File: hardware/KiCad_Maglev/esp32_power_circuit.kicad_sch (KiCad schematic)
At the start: 9 parts

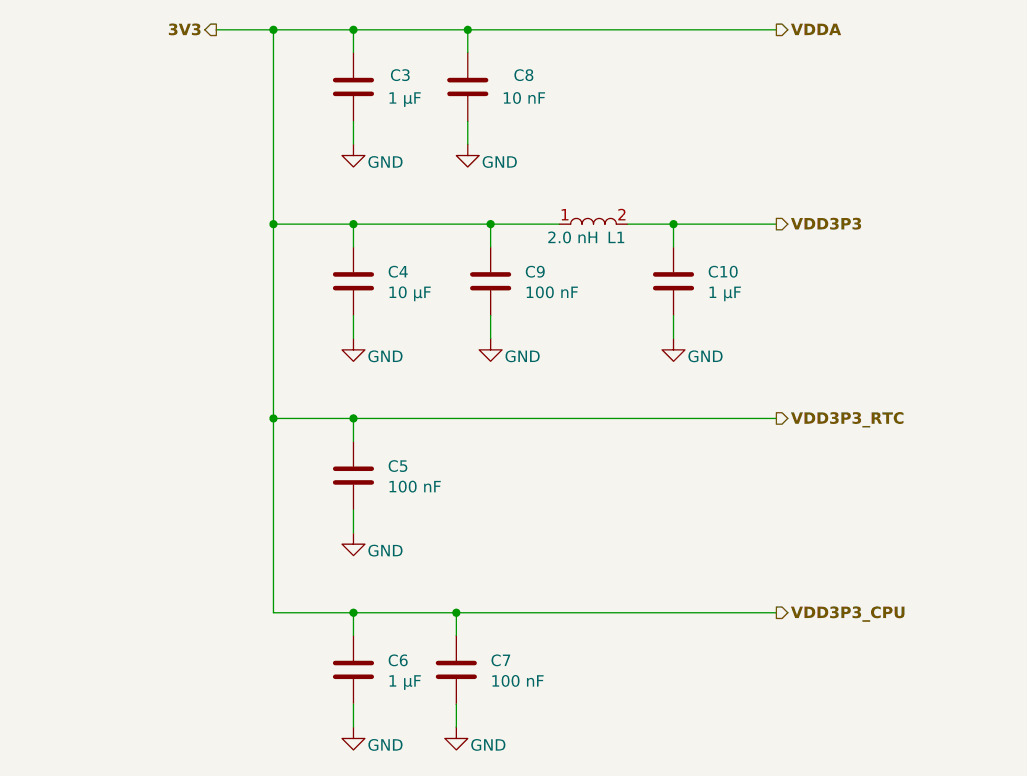
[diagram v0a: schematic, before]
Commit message: Added Footprints/Models for coil and ringmagnet, changed most components to 1206 series
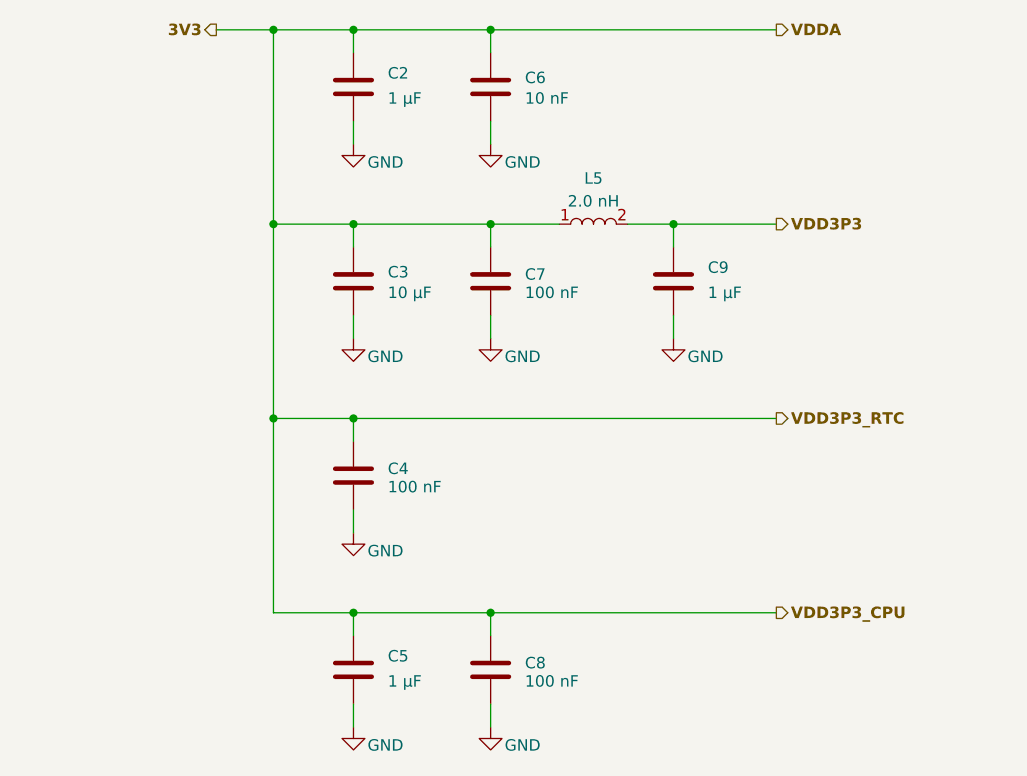
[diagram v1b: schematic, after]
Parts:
- removed C10, C3, C6: 0805_H1.25_R_885012107015, Capacitor_SMD_Wurth:C_Wurth_WCAP-CSGP-0805_H1.25_R, symbol Capacitor_Wurth_WCAP-CSGP:0805_H1.25_R_885012107015
- removed C5, C7, C9: 1812_H1.25_885012210008, Capacitor_SMD_Wurth:C_Wurth_WCAP-CSGP-1812_H1.25, symbol Capacitor_Wurth_WCAP-CSGP:1812_H1.25_885012210008
- removed C8: 0402_885012205050, Capacitor_SMD_Wurth:C_Wurth_WCAP-CSGP-0402, symbol Capacitor_Wurth_WCAP-CSGP:0402_885012205050
- removed L1: 0402_744765020A, Inductor_SMD_Wurth:L_Wurth_WE-KI-0402, symbol Inductor_Wurth_WE-KI:0402_744765020A
- added C2, C5, C9: 1206_H1.6_885012208093, Capacitor_SMD_Wurth:C_Wurth_WCAP-CSGP-1206_H1.6, symbol Capacitor_Wurth_WCAP-CSGP:1206_H1.6_885012208093
- added C4, C7, C8: 1206_H1.25_885012208118, Capacitor_SMD_Wurth:C_Wurth_WCAP-CSGP-1206_H1.25, symbol Capacitor_Wurth_WCAP-CSGP:1206_H1.25_885012208118
- added C6: 1206_H1.25_885012008055, Capacitor_SMD_Wurth:C_Wurth_WCAP-CSGP-1206_H1.25, symbol Capacitor_Wurth_WCAP-CSGP:1206_H1.25_885012008055
- added L5: 0603_744761020A, Inductor_SMD_Wurth:L_Wurth_WE-KI-0603, symbol Inductor_Wurth_WE-KI:0603_744761020A
- renumbered C4 to C3
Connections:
- net 3V3: now also C2.1, C4.1, C5.1, C6.1, C7.1, C8.1, L5.1
- net GND: now also C2.2, C4.2, C5.2, C6.2, C7.2, C8.2, C9.2
- net VDD3P3: now also C9.1, L5.2

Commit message: changed mounting and spacing system and  some detail changes
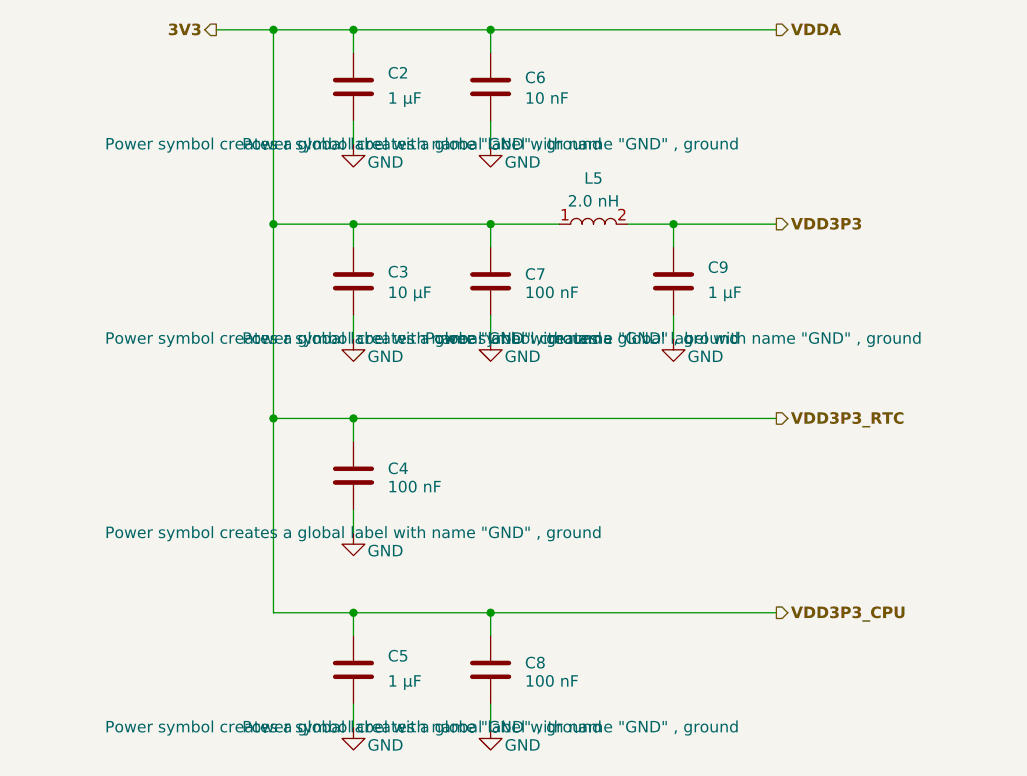
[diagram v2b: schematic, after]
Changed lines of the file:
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@@
 			)
 		)
-		(property "Description" ""
+		(property "Description" "Power symbol creates a global label with name \"GND\" , ground"
 			(at 168.91 91.44 0)
 			(show_name no)
@@
 			)
 		)
-		(property "Description" ""
+		(property "Description" "Power symbol creates a global label with name \"GND\" , ground"
 			(at 148.59 134.62 0)
 			(show_name no)
@@
 			)
 		)
-		(property "Description" ""
+		(property "Description" "Power symbol creates a global label with name \"GND\" , ground"
 			(at 133.35 91.44 0)
 			(show_name no)
@@
 			)
 		)
-		(property "Description" ""
+		(property "Description" "Power symbol creates a global label with name \"GND\" , ground"
 			(at 148.59 69.85 0)
 			(show_name no)
@@
 			)
 		)
-		(property "Description" ""
+		(property "Description" "Power symbol creates a global label with name \"GND\" , ground"
 			(at 133.35 134.62 0)
 			(show_name no)
@@
 			)
 		)
-		(property "Description" ""
+		(property "Description" "Power symbol creates a global label with name \"GND\" , ground"
 			(at 133.35 113.03 0)
 			(show_name no)
@@
 			)
 		)
-		(property "Description" ""
+		(property "Description" "Power symbol creates a global label with name \"GND\" , ground"
 			(at 133.35 69.85 0)
 			(show_name no)
@@
 			)
 		)
-		(property "Description" ""
+		(property "Description" "Power symbol creates a global label with name \"GND\" , ground"
 			(at 148.59 91.44 0)
 			(show_name no)
